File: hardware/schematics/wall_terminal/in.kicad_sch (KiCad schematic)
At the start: 9 parts

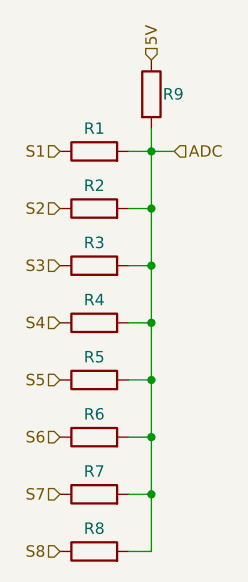
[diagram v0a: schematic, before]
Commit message: fix: added optional resistors on PWM outputs.
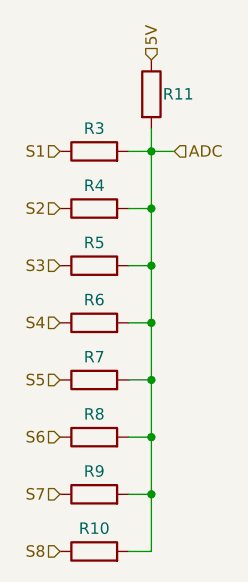
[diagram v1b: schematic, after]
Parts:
- renumbered R8 to R10, R9 to R11, R1 to R3, R2 to R4, R3 to R5, R4 to R6, R5 to R7, R6 to R8, R7 to R9

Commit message: chore: added optimal voltage divider resistor's values.
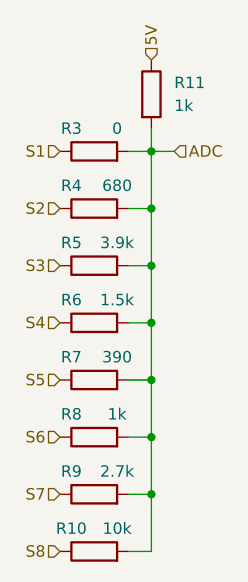
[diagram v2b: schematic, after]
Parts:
- R10: value R -> 10k
- R11, R8: value R -> 1k
- R3: value R -> 0
- R4: value R -> 680
- R5: value R -> 3.9k
- R6: value R -> 1.5k
- R7: value R -> 390
- R9: value R -> 2.7k
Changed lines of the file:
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@@
 		(dnp no)
 		(property "Reference" "R11"
-			(at 140.97 69.85 0)
+			(at 142.24 68.58 0)
 			(effects
 				(font
@@
 			)
 		)
-		(property "Value" "R"
+		(property "Value" "1k"
 			(at 142.24 71.1199 0)
 			(effects
@@
 				)
 				(justify left)
-				(hide yes)
 			)
 		)
@@
 		(dnp no)
 		(property "Reference" "R6"
-			(at 133.35 92.71 90)
-			(effects
-				(font
-					(size 1.27 1.27)
-				)
-			)
-		)
-		(property "Value" "R"
-			(at 133.35 91.44 90)
-			(effects
-				(font
-					(size 1.27 1.27)
-				)
-				(hide yes)
+			(at 130.81 92.71 90)
+			(effects
+				(font
+					(size 1.27 1.27)
+				)
+			)
+		)
+		(property "Value" "1.5k"
+			(at 135.89 92.71 90)
+			(effects
+				(font
+					(size 1.27 1.27)
+				)
 			)
 		)
@@
 		(dnp no)
 		(property "Reference" "R7"
-			(at 133.35 99.06 90)
-			(effects
-				(font
-					(size 1.27 1.27)
-				)
-			)
-		)
-		(property "Value" "R"
-			(at 133.35 97.79 90)
-			(effects
-				(font
-					(size 1.27 1.27)
-				)
-				(hide yes)
+			(at 130.81 99.06 90)
+			(effects
+				(font
+					(size 1.27 1.27)
+				)
+			)
+		)
+		(property "Value" "390"
+			(at 135.89 99.06 90)
+			(effects
+				(font
+					(size 1.27 1.27)
+				)
 			)
 		)
@@
 		(dnp no)
 		(property "Reference" "R4"
-			(at 133.35 80.01 90)
-			(effects
-				(font
-					(size 1.27 1.27)
-				)
-			)
-		)
-		(property "Value" "R"
-			(at 133.35 78.74 90)
-			(effects
-				(font
-					(size 1.27 1.27)
-				)
-				(hide yes)
+			(at 130.81 80.01 90)
+			(effects
+				(font
+					(size 1.27 1.27)
+				)
+			)
+		)
+		(property "Value" "680"
+			(at 135.89 80.01 90)
+			(effects
+				(font
+					(size 1.27 1.27)
+				)
 			)
 		)
@@
 		(dnp no)
 		(property "Reference" "R5"
-			(at 133.35 86.36 90)
-			(effects
-				(font
-					(size 1.27 1.27)
-				)
-			)
-		)
-		(property "Value" "R"
-			(at 133.35 85.09 90)
-			(effects
-				(font
-					(size 1.27 1.27)
-				)
-				(hide yes)
+			(at 130.81 86.36 90)
+			(effects
+				(font
+					(size 1.27 1.27)
+				)
+			)
+		)
+		(property "Value" "3.9k"
+			(at 135.89 86.36 90)
+			(effects
+				(font
+					(size 1.27 1.27)
+				)
 			)
 		)
@@
 		(dnp no)
 		(property "Reference" "R9"
-			(at 133.35 111.76 90)
-			(effects
-				(font
-					(size 1.27 1.27)
-				)
-			)
-		)
-		(property "Value" "R"
-			(at 133.35 110.49 90)
-			(effects
-				(font
-					(size 1.27 1.27)
-				)
-				(hide yes)
+			(at 130.81 111.76 90)
+			(effects
+				(font
+					(size 1.27 1.27)
+				)
+			)
+		)
+		(property "Value" "2.7k"
+			(at 135.89 111.76 90)
+			(effects
+				(font
+					(size 1.27 1.27)
+				)
 			)
 		)
@@
 		(dnp no)
 		(property "Reference" "R10"
-			(at 133.35 118.11 90)
-			(effects
-				(font
-					(size 1.27 1.27)
-				)
-			)
-		)
-		(property "Value" "R"
-			(at 133.35 116.84 90)
-			(effects
-				(font
-					(size 1.27 1.27)
-				)
-				(hide yes)
+			(at 130.81 118.11 90)
+			(effects
+				(font
+					(size 1.27 1.27)
+				)
+			)
+		)
+		(property "Value" "10k"
+			(at 135.89 118.11 90)
+			(effects
+				(font
+					(size 1.27 1.27)
+				)
 			)
 		)
@@
 		(dnp no)
 		(property "Reference" "R8"
-			(at 133.35 105.41 90)
-			(effects
-				(font
-					(size 1.27 1.27)
-				)
-			)
-		)
-		(property "Value" "R"
-			(at 133.35 104.14 90)
-			(effects
-				(font
-					(size 1.27 1.27)
-				)
-				(hide yes)
+			(at 130.81 105.41 90)
+			(effects
+				(font
+					(size 1.27 1.27)
+				)
+			)
+		)
+		(property "Value" "1k"
+			(at 135.89 105.41 90)
+			(effects
+				(font
+					(size 1.27 1.27)
+				)
 			)
 		)
@@
 		(dnp no)
 		(property "Reference" "R3"
-			(at 133.35 73.66 90)
-			(effects
-				(font
-					(size 1.27 1.27)
-				)
-			)
-		)
-		(property "Value" "R"
-			(at 133.35 72.39 90)
-			(effects
-				(font
-					(size 1.27 1.27)
-				)
-				(hide yes)
-			)
-		)
+			(at 130.81 73.66 90)
+			(effects
+				(font
+					(size 1.27 1.27)
+				)
+			)
+		)
+		(property "Value" "0"
+			(at 135.89 73.66 90)
+			(effects
+				(font
+					(size 1.27 1.27)
+				)
+			)
+		)
